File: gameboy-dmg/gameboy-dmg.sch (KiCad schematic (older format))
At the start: 16 parts, among them J1 Conn_01x02, J2 Conn_01x06, J3 Conn_01x02, SW1 SW_Push, SW2 SW_Push, SW3 SW_Push, SW4 SW_Push, SW5 SW_Push, SW6 SW_Push, SW7 SW_Push, SW8 SW_Push, U1 MCP23017_SO

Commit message: Added some graphics and stuffs
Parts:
- C1: value C_Small -> 33nF
- C2: value C_Small -> 10uF
- R1: value R -> 270R
- R2: value R -> 150R
- renumbered SW8 to A, SW7 to B, SW3 to DOWN, SW1 to LEFT, SW4 to RIGHT, SW5 to SELECT, SW6 to START, SW2 to UP
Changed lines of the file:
@@
 $EndDescr
 $Comp
-L Switch:SW_Push SW2
+L Switch:SW_Push UP
 U 1 1 5E7D2D40
 P 2250 3050
-F 0 "SW2" H 2250 3335 50  0000 C CNN
+F 0 "UP" H 2250 3335 50  0000 C CNN
 F 1 "SW_Push" H 2250 3244 50  0000 C CNN
 F 2 "pad:GAMEBOY_BUTTON_PAD-D6MM" H 2250 3250 50  0001 C CNN
@@
 $EndComp
 $Comp
-L Switch:SW_Push SW1
+L Switch:SW_Push LEFT
 U 1 1 5E7D31A2
 P 1650 3600
-F 0 "SW1" H 1650 3885 50  0000 C CNN
+F 0 "LEFT" H 1650 3885 50  0000 C CNN
 F 1 "SW_Push" H 1650 3794 50  0000 C CNN
 F 2 "pad:GAMEBOY_BUTTON_PAD-D6MM" H 1650 3800 50  0001 C CNN
@@
 $EndComp
 $Comp
-L Switch:SW_Push SW3
+L Switch:SW_Push DOWN
 U 1 1 5E7D3644
 P 2450 4350
-F 0 "SW3" H 2450 4635 50  0000 C CNN
+F 0 "DOWN" H 2450 4635 50  0000 C CNN
 F 1 "SW_Push" H 2450 4544 50  0000 C CNN
 F 2 "pad:GAMEBOY_BUTTON_PAD-D6MM" H 2450 4550 50  0001 C CNN
@@
 $EndComp
 $Comp
-L Switch:SW_Push SW4
+L Switch:SW_Push RIGHT
 U 1 1 5E7D37A1
 P 3000 3850
-F 0 "SW4" H 3000 4135 50  0000 C CNN
+F 0 "RIGHT" H 3000 4135 50  0000 C CNN
 F 1 "SW_Push" H 3000 4044 50  0000 C CNN
 F 2 "pad:GAMEBOY_BUTTON_PAD-D6MM" H 3000 4050 50  0001 C CNN
@@
 $EndComp
 $Comp
-L Switch:SW_Push SW5
+L Switch:SW_Push SELECT
 U 1 1 5E7D3981
 P 3950 5250
-F 0 "SW5" H 3950 5535 50  0000 C CNN
+F 0 "SELECT" H 3950 5535 50  0000 C CNN
 F 1 "SW_Push" H 3950 5444 50  0000 C CNN
 F 2 "pad:GAMEBOY_BUTTON_PAD-DUAL_D4MM" H 3950 5450 50  0001 C CNN
@@
 $EndComp
 $Comp
-L Switch:SW_Push SW6
+L Switch:SW_Push START
 U 1 1 5E7D3B02
 P 4800 5000
-F 0 "SW6" H 4800 5285 50  0000 C CNN
+F 0 "START" H 4800 5285 50  0000 C CNN
 F 1 "SW_Push" H 4800 5194 50  0000 C CNN
 F 2 "pad:GAMEBOY_BUTTON_PAD-DUAL_D4MM" H 4800 5200 50  0001 C CNN
@@
 $EndComp
 $Comp
-L Switch:SW_Push SW7
+L Switch:SW_Push B
 U 1 1 5E7D3D72
 P 5500 4150
-F 0 "SW7" H 5500 4435 50  0000 C CNN
+F 0 "B" H 5500 4435 50  0000 C CNN
 F 1 "SW_Push" H 5500 4344 50  0000 C CNN
 F 2 "pad:GAMEBOY_BUTTON_PAD-D6MM" H 5500 4350 50  0001 C CNN
@@
 $EndComp
 $Comp
-L Switch:SW_Push SW8
+L Switch:SW_Push A
 U 1 1 5E7D3F12
 P 6250 3650
-F 0 "SW8" H 6250 3935 50  0000 C CNN
+F 0 "A" H 6250 3935 50  0000 C CNN
 F 1 "SW_Push" H 6250 3844 50  0000 C CNN
 F 2 "pad:GAMEBOY_BUTTON_PAD-D6MM" H 6250 3850 50  0001 C CNN
@@
 P 3000 1550
 F 0 "R1" V 2793 1550 50  0000 C CNN
-F 1 "R" V 2884 1550 50  0000 C CNN
+F 1 "270R" V 2884 1550 50  0000 C CNN
 F 2 "Resistor_SMD:R_0603_1608Metric" V 2930 1550 50  0001 C CNN
 F 3 "~" H 3000 1550 50  0001 C CNN
@@
 P 3800 1750
 F 0 "R2" H 3730 1704 50  0000 R CNN
-F 1 "R" H 3730 1795 50  0000 R CNN
+F 1 "150R" H 3730 1795 50  0000 R CNN
 F 2 "Resistor_SMD:R_0603_1608Metric" V 3730 1750 50  0001 C CNN
 F 3 "~" H 3800 1750 50  0001 C CNN
@@
 P 3400 1750
 F 0 "C1" H 3492 1796 50  0000 L CNN
-F 1 "C_Small" H 3492 1705 50  0000 L CNN
+F 1 "33nF" H 3492 1705 50  0000 L CNN
 F 2 "Capacitor_SMD:C_0603_1608Metric" H 3400 1750 50  0001 C CNN
 F 3 "~" H 3400 1750 50  0001 C CNN
@@
 P 4150 1550
 F 0 "C2" V 3921 1550 50  0000 C CNN
-F 1 "C_Small" V 4012 1550 50  0000 C CNN
+F 1 "10uF" V 4012 1550 50  0000 C CNN
 F 2 "Capacitor_THT:CP_Radial_D5.0mm_P2.00mm" H 4150 1550 50  0001 C CNN
 F 3 "~" H 4150 1550 50  0001 C CNN

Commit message: Added some more bits
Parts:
- removed J2: Conn_01x06, Connector_PinHeader_2.54mm:PinHeader_1x06_P2.54mm_Vertical, symbol Connector_Generic:Conn_01x06
- added D1: LED, LED_SMD:LED_0603_1608Metric, symbol Device:LED
- added D2: LED, LED_THT:LED_D3.0mm, symbol Device:LED
- added J2, J4: Conn_01x02, Connector_PinHeader_2.54mm:PinHeader_1x02_P2.54mm_Vertical, symbol Connector_Generic:Conn_01x02
- added J5: Raspberry_Pi_2_3, Connector_PinHeader_2.54mm:PinHeader_2x20_P2.54mm_Vertical, symbol Connector:Raspberry_Pi_2_3
- added J6: Conn_01x09, Connector_PinHeader_2.54mm:PinHeader_1x09_P2.54mm_Vertical, symbol Connector_Generic:Conn_01x09
- added JP1, JP7: SolderJumper_2_Bridged, Jumper:SolderJumper-2_P1.3mm_Bridged_RoundedPad1.0x1.5mm, symbol Jumper:SolderJumper_2_Bridged
- added JP2, JP3, JP4, JP5, JP6: SolderJumper_2_Open, Jumper:SolderJumper-2_P1.3mm_Open_RoundedPad1.0x1.5mm, symbol Jumper:SolderJumper_2_Open
- added R3: R_Small, Resistor_SMD:R_0603_1608Metric, symbol Device:R_Small
- added SW1: SW_DIP_x01, Connector_PinHeader_2.54mm:PinHeader_1x02_P2.54mm_Vertical, symbol Switch:SW_DIP_x01
- renumbered A to A1, B to B1, DOWN to DOWN1, LEFT to LEFT1, RIGHT to RIGHT1, SELECT to SELECT1, START to START1, UP to UP1
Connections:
- net labels added: +3.3V, GPIO_INTA, GPIO_INTA_PI, GPIO_INTB, GPIO_INTB_PI, GPIO_SCK, GPIO_SCK_PI, GPIO_SDA, GPIO_SDA_PI, TFT_BACKLIGHT, TFT_BACKLIGHT_GPIO, TFT_BACKLIGHT_Vcc, TFT_CS, TFT_DC, TFT_MISO, TFT_MOSI, TFT_RESET, TFT_SCK
- wire segments 64 -> 93
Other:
- note added: "2.4 TFT ILI9341 Screen"
- note added: "Battery Connection\n"
- moved on the sheet: A1, B1, C1, C2, DOWN1, J1, J3, LEFT1, R1, R2, RIGHT1, SELECT1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

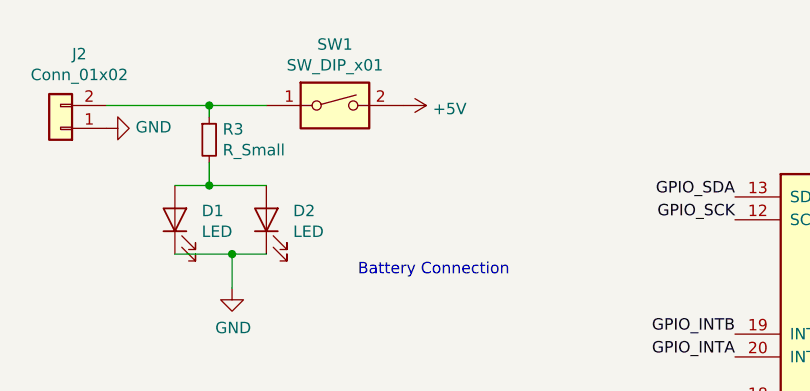
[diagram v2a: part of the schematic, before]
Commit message: Fixed some missing holes
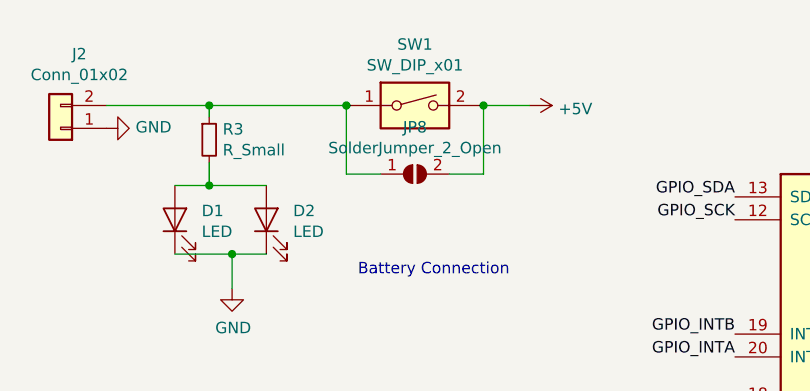
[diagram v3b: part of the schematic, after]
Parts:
- added JP8: SolderJumper_2_Open, Jumper:SolderJumper-2_P1.3mm_Open_RoundedPad1.0x1.5mm, symbol Jumper:SolderJumper_2_Open
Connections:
- net +5V: now also JP8.2 (B)
- net at J2.2 (Pin_2), R3.1, SW1.1: now also JP8.1 (A)
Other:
- moved on the sheet: SW1
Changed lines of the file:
@@
 	8700 2850 9050 2850
-$Comp
-L power:+5V #PWR0113
-U 1 1 5E7ECABF
-P 5850 850
-F 0 "#PWR0113" H 5850 700 50  0001 C CNN
-F 1 "+5V" V 5865 978 50  0000 L CNN
-F 2 "" H 5850 850 50  0001 C CNN
-F 3 "" H 5850 850 50  0001 C CNN
-	1    5850 850
-	0    1    1    0
-$EndComp
 $Comp
 L power:GND #PWR0114
@@
 	5000 900  5000 850
 Connection ~ 5000 850
-Wire Wire Line
-	5000 850  5250 850
 $Comp
 L Switch:SW_DIP_x01 SW1
 U 1 1 5EA31C48
-P 5550 850
-F 0 "SW1" H 5550 1117 50  0000 C CNN
-F 1 "SW_DIP_x01" H 5550 1026 50  0000 C CNN
-F 2 "Connector_PinHeader_2.54mm:PinHeader_1x02_P2.54mm_Vertical" H 5550 850 50  0001 C CNN
-F 3 "~" H 5550 850 50  0001 C CNN
-	1    5550 850
-	1    0    0    -1
-$EndComp
+P 5900 850
+F 0 "SW1" H 5900 1117 50  0000 C CNN
+F 1 "SW_DIP_x01" H 5900 1026 50  0000 C CNN
+F 2 "Connector_PinHeader_2.54mm:PinHeader_1x02_P2.54mm_Vertical" H 5900 850 50  0001 C CNN
+F 3 "~" H 5900 850 50  0001 C CNN
+	1    5900 850
+	1    0    0    -1
+$EndComp
+$Comp
+L power:+5V #PWR0113
+U 1 1 5E7ECABF
+P 6400 850
+F 0 "#PWR0113" H 6400 700 50  0001 C CNN
+F 1 "+5V" V 6415 978 50  0000 L CNN
+F 2 "" H 6400 850 50  0001 C CNN
+F 3 "" H 6400 850 50  0001 C CNN
+	1    6400 850
+	0    1    1    0
+$EndComp
+$Comp
+L Jumper:SolderJumper_2_Open JP8
+U 1 1 5EA3FFE3
+P 5900 1150
+F 0 "JP8" H 5900 1355 50  0000 C CNN
+F 1 "SolderJumper_2_Open" H 5900 1264 50  0000 C CNN
+F 2 "Jumper:SolderJumper-2_P1.3mm_Open_RoundedPad1.0x1.5mm" H 5900 1150 50  0001 C CNN
+F 3 "~" H 5900 1150 50  0001 C CNN
+	1    5900 1150
+	1    0    0    -1
+$EndComp
+Wire Wire Line
+	5000 850  5600 850
+Wire Wire Line
+	5600 850  5600 1150
+Wire Wire Line
+	5600 1150 5750 1150
+Connection ~ 5600 850
+Wire Wire Line
+	6050 1150 6200 1150
+Wire Wire Line
+	6200 1150 6200 850
+Wire Wire Line
+	6200 850  6400 850
+Connection ~ 6200 850
 $EndSCHEMATC

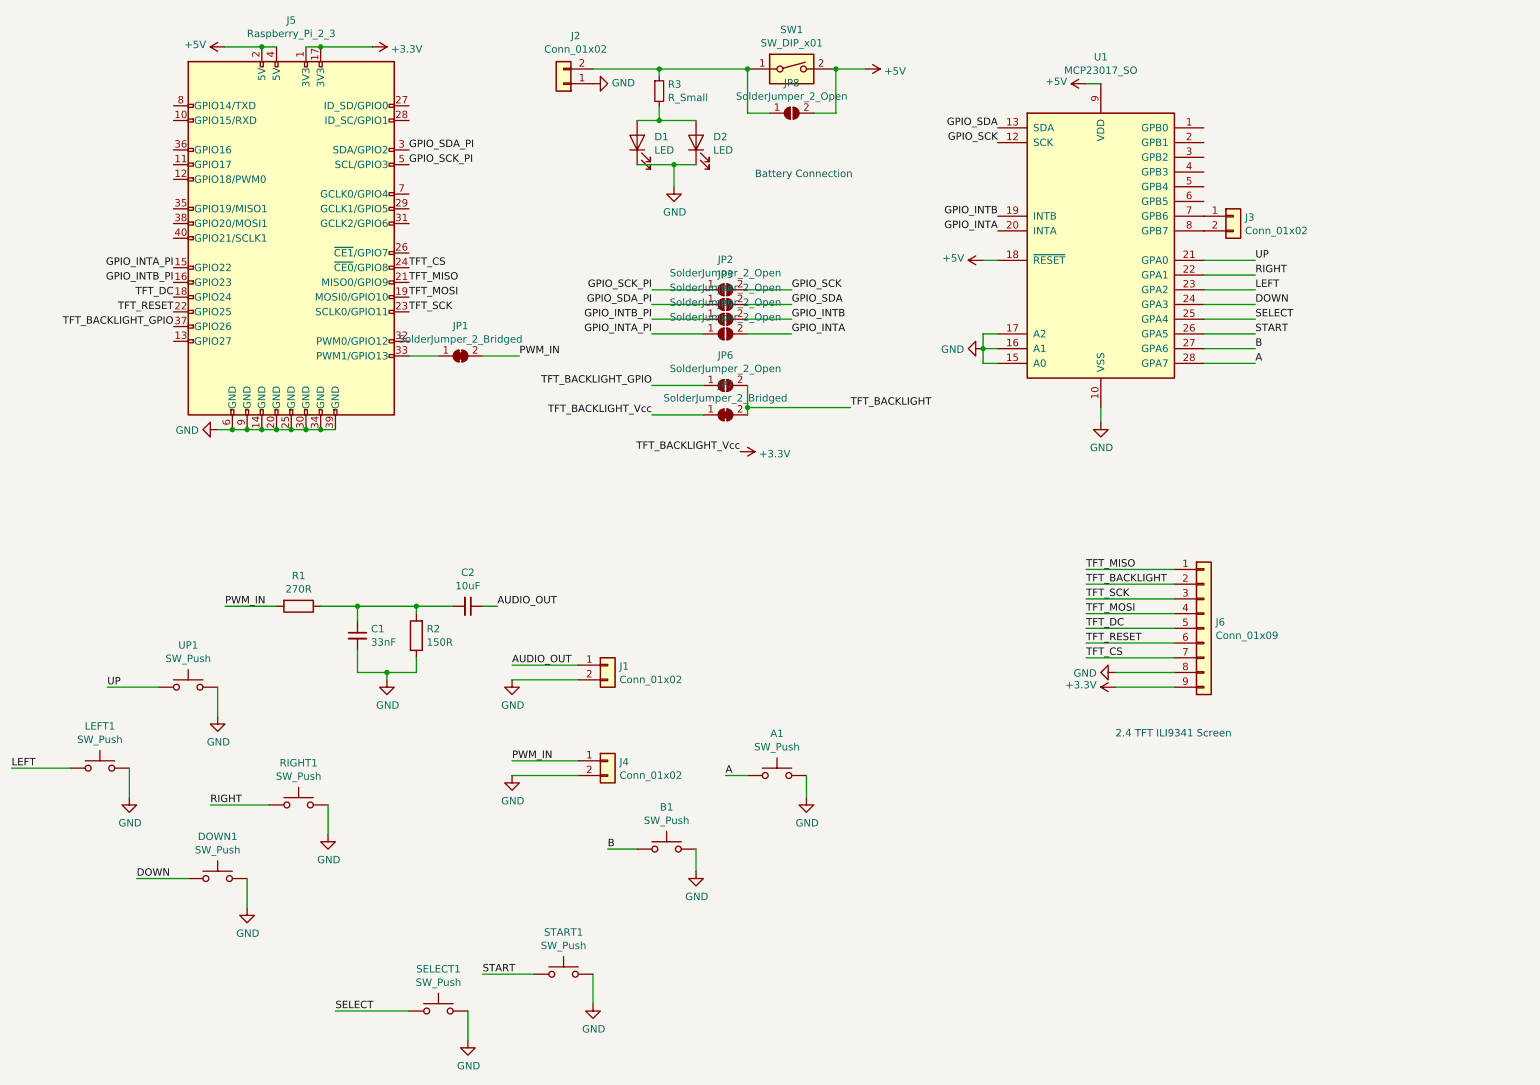
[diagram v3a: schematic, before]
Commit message: Rough lipo charger and 5v boost added
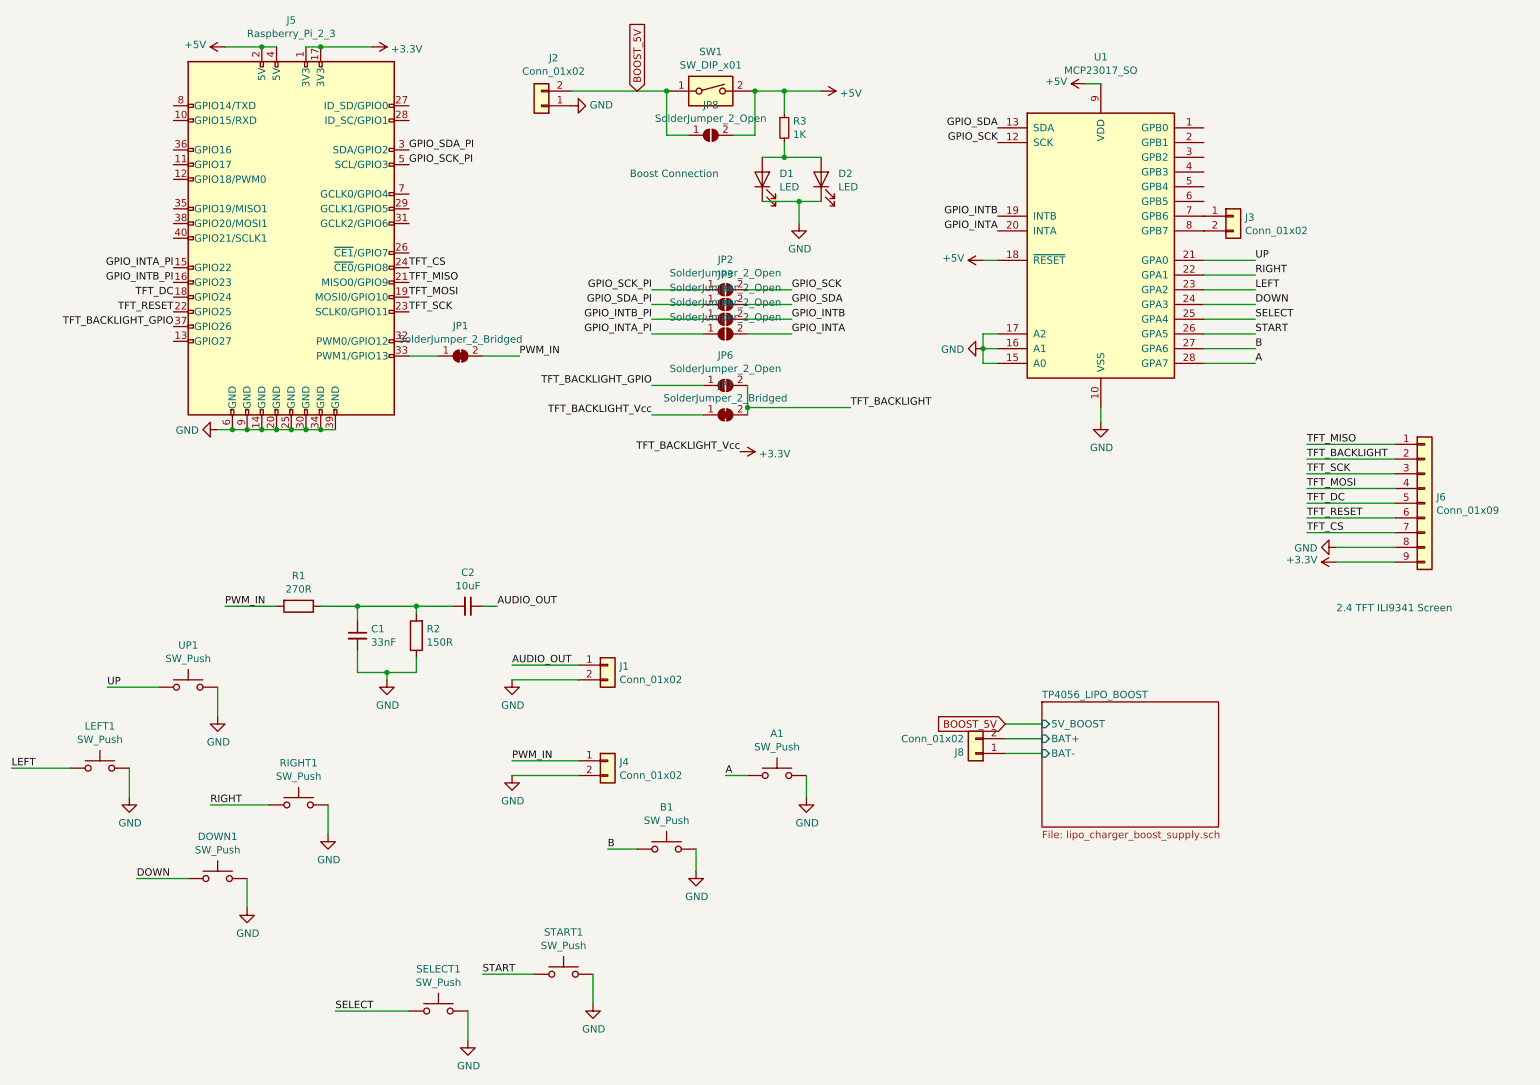
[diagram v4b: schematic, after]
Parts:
- added J8: Conn_01x02, Connector_PinHeader_2.54mm:PinHeader_1x02_P2.54mm_Vertical, symbol Connector_Generic:Conn_01x02
- R3: value R_Small -> 1K
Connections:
- net +5V: now also R3.1
- net BOOST_5V: now reaches J2.2 (Pin_2), JP8.1 (A), SW1.1
- net BOOST_5V: no longer R3.1
- new net TP4056_LIPO_BOOST/BAT+: J8.2 (Pin_2)
- new net TP4056_LIPO_BOOST/BAT-: J8.1 (Pin_1)
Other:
- note added: "Boost Connection"
- note removed: "Battery Connection\n"
- moved on the sheet: D1, D2, J2, J6, JP8, R3, SW1

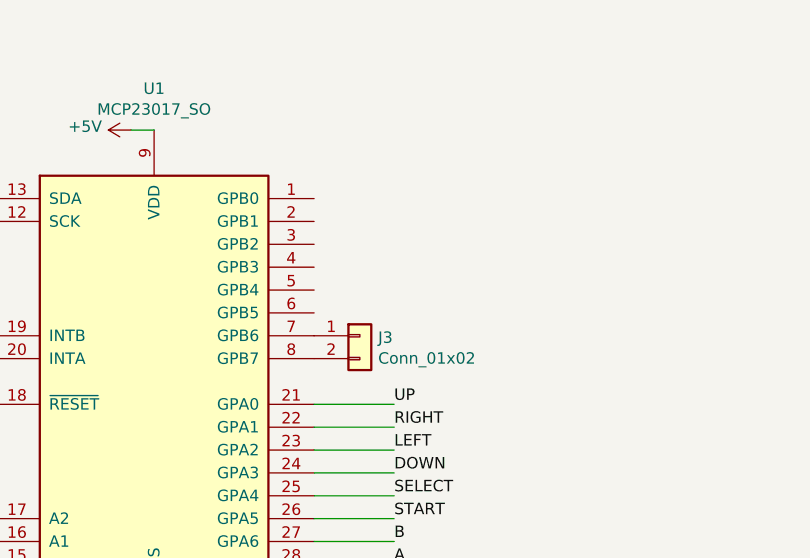
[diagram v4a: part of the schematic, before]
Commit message: Broke out all of port B to extenal pins from the MSP GPIO expander
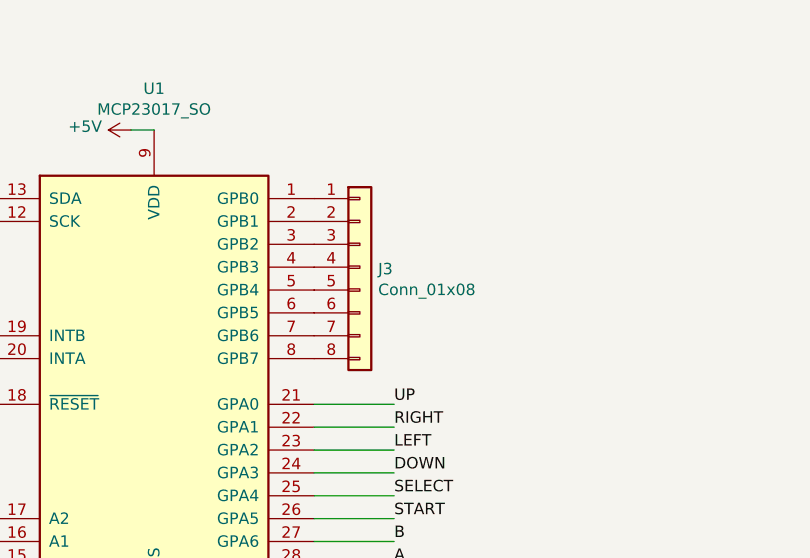
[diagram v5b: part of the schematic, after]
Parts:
- removed J3: Conn_01x02, Connector_PinHeader_2.54mm:PinHeader_1x02_P2.54mm_Vertical, symbol Connector_Generic:Conn_01x02
- added J3: Conn_01x08, Connector_PinHeader_2.54mm:PinHeader_1x08_P2.54mm_Vertical, symbol Connector_Generic:Conn_01x08
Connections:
- net at U1.1 (GPB0): now also J3.1 (Pin_1)
- net at U1.2 (GPB1): now also J3.2 (Pin_2)
- net at U1.3 (GPB2): now also J3.3 (Pin_3)
- net at U1.4 (GPB3): now also J3.4 (Pin_4)
- net at U1.5 (GPB4): now also J3.5 (Pin_5)
- net at U1.6 (GPB5): now also J3.6 (Pin_6)
- net at U1.7 (GPB6): now also J3.7 (Pin_7)
- net at U1.8 (GPB7): now also J3.8 (Pin_8)
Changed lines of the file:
@@
 Text Label 9050 2350 0    50   ~ 0
 LEFT
-$Comp
-L Connector_Generic:Conn_01x02 J3
-U 1 1 5E81943F
-P 8900 1850
-F 0 "J3" H 8980 1842 50  0000 L CNN
-F 1 "Conn_01x02" H 8980 1751 50  0000 L CNN
-F 2 "Connector_PinHeader_2.54mm:PinHeader_1x02_P2.54mm_Vertical" H 8900 1850 50  0001 C CNN
-F 3 "~" H 8900 1850 50  0001 C CNN
-	1    8900 1850
-	1    0    0    -1
-$EndComp
 Text Label 9050 2650 0    50   ~ 0
 START
@@
 	4400 1000 5050 1000
 Connection ~ 5050 1000
+$Comp
+L Connector_Generic:Conn_01x08 J3
+U 1 1 5E9A7474
+P 8900 1550
+F 0 "J3" H 8980 1542 50  0000 L CNN
+F 1 "Conn_01x08" H 8980 1451 50  0000 L CNN
+F 2 "Connector_PinHeader_2.54mm:PinHeader_1x08_P2.54mm_Vertical" H 8900 1550 50  0001 C CNN
+F 3 "~" H 8900 1550 50  0001 C CNN
+	1    8900 1550
+	1    0    0    -1
+$EndComp
 $EndSCHEMATC
